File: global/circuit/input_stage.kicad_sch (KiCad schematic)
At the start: 9 parts, among them U3 TL081H

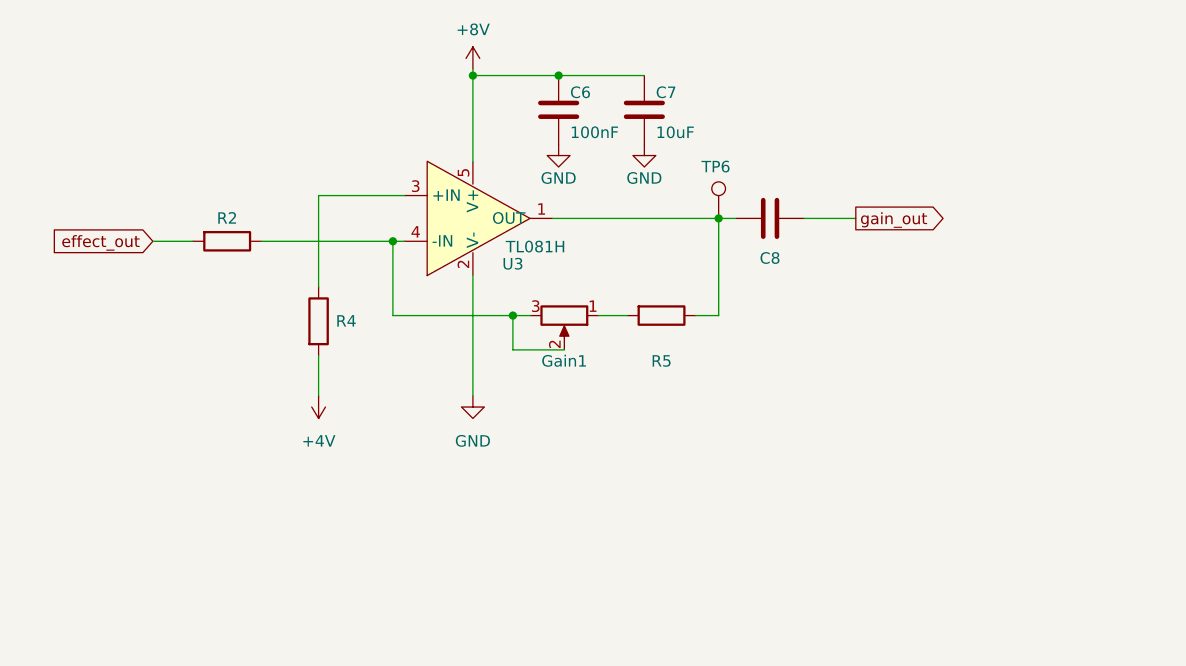
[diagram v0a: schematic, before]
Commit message: rework distortion circuit and simulations
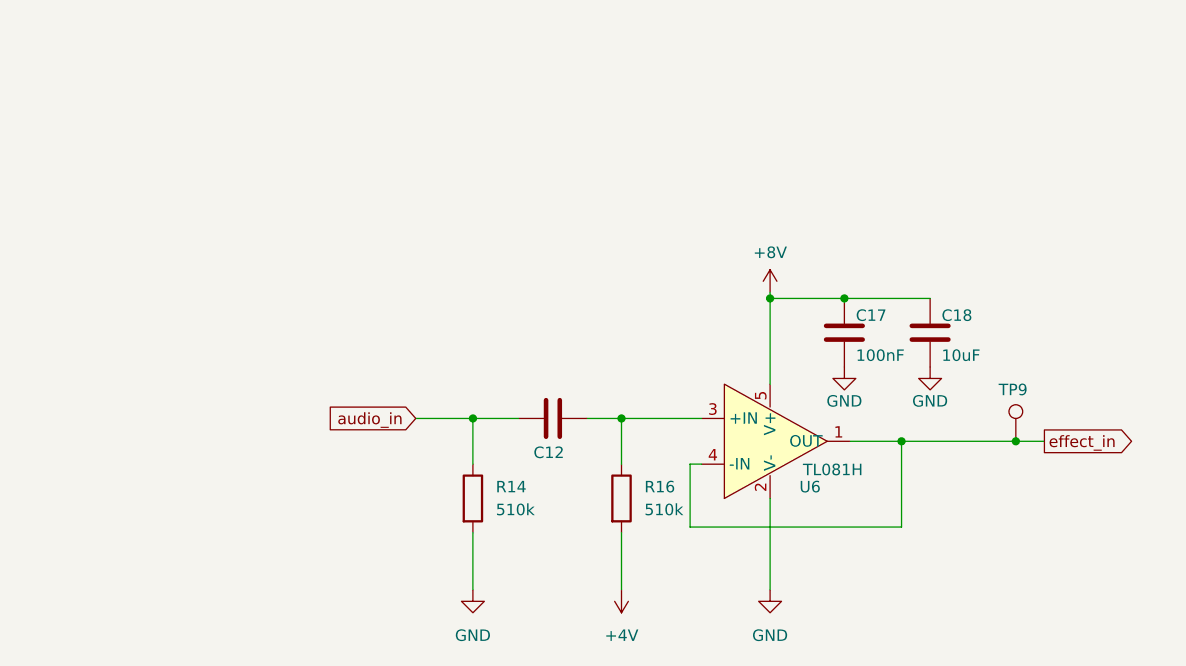
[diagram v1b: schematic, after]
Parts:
- removed C6: 100nF, Capacitor_SMD:C_0805_2012Metric_Pad1.18x1.45mm_HandSolder, symbol Device:C
- removed C7: 10uF, Capacitor_SMD:C_0805_2012Metric_Pad1.18x1.45mm_HandSolder, symbol Device:C
- removed C8: C, Capacitor_SMD:C_0805_2012Metric_Pad1.18x1.45mm_HandSolder, symbol Device:C
- removed Gain1: 10k, Connector_PinHeader_2.54mm:PinHeader_1x03_P2.54mm_Vertical, symbol Device:R_Potentiometer
- removed R2, R4, R5: R, Resistor_SMD:R_0805_2012Metric_Pad1.20x1.40mm_HandSolder, symbol Device:R
- removed TP6: TestPoint, TestPoint:TestPoint_THTPad_1.0x1.0mm_Drill0.5mm, symbol Connector:TestPoint
- removed U3: TL081H, Package_TO_SOT_SMD:SOT-23-5_HandSoldering, symbol Amplifier_Operational:TL081H
- added C12: 22uF, Capacitor_SMD:C_1206_3216Metric_Pad1.33x1.80mm_HandSolder, symbol Device:C
- added C17: 100nF, Capacitor_SMD:C_0805_2012Metric_Pad1.18x1.45mm_HandSolder, symbol Device:C
- added C18: 10uF, Capacitor_SMD:C_0805_2012Metric_Pad1.18x1.45mm_HandSolder, symbol Device:C
- added R14, R16: 510k, Resistor_SMD:R_0805_2012Metric_Pad1.20x1.40mm_HandSolder, symbol Device:R
- added TP9: TestPoint, TestPoint:TestPoint_THTPad_1.0x1.0mm_Drill0.5mm, symbol Connector:TestPoint
- added U6: TL081H, Package_TO_SOT_SMD:SOT-23-5_HandSoldering, symbol Amplifier_Operational:TL081H
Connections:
- net +4V: now also R16.2
- net +8V: now also C17.1, C18.1, U6.5 (V+)
- net GND: now also C17.2, C18.2, R14.2, U6.2 (V-)
- new net: C12.2, R16.1, U6.3 (+IN)
- new net audio_in: C12.1, R14.1
- new net effect_in: TP9.1, U6.1 (OUT), U6.4 (-IN)
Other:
- title: Gain Stage -> (none)

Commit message: create gerber files, update BOM for REV2
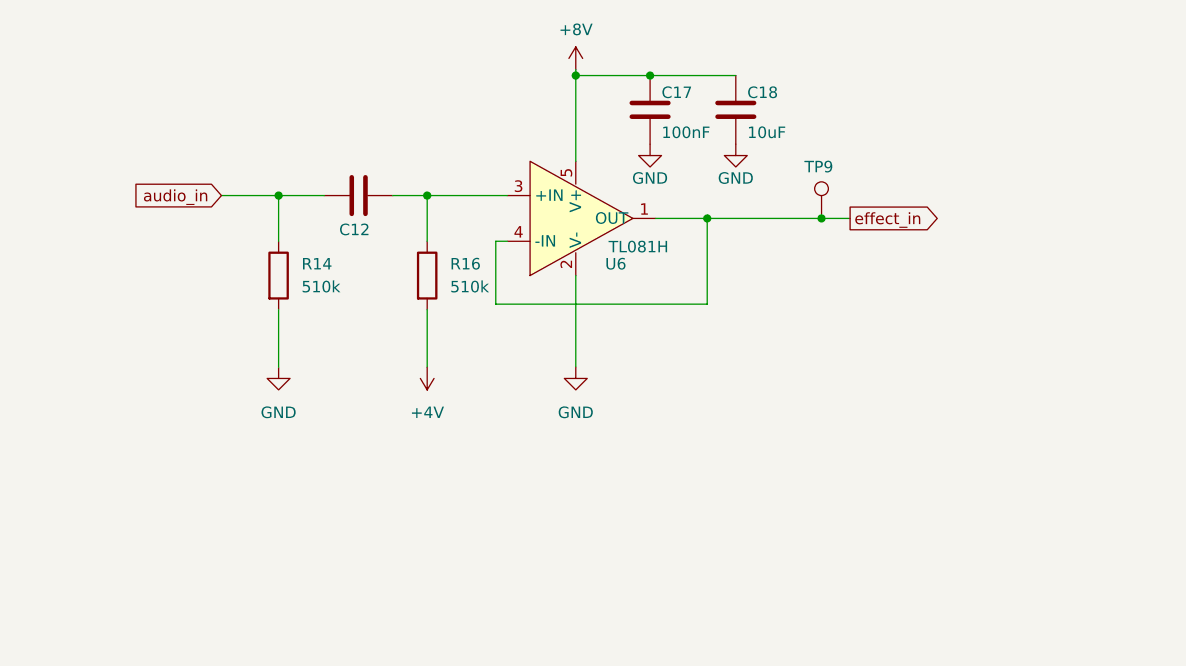
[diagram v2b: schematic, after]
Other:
- title: (none) -> Input stage
- moved on the sheet: C12, C17, C18, R14, R16, TP9, U6

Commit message: rework global circuits
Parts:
- renumbered C18 to C?, C17 to C?, C12 to C?, R16 to R?, R14 to R?, TP9 to TP?, U6 to U?
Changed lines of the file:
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@@
   (symbol (lib_id "power:+4V") (at 96.52 70.485 180) (unit 1)
     (in_bom yes) (on_board yes) (fields_autoplaced)
-    (property "Reference" "#PWR0116" (id 0) (at 96.52 66.675 0)
+    (property "Reference" "#PWR?" (id 0) (at 96.52 66.675 0)
       (effects (font (size 1.27 1.27)) hide)
     )
@@
   (symbol (lib_id "Device:C") (at 130.81 41.91 0) (unit 1)
     (in_bom yes) (on_board yes)
-    (property "Reference" "C18" (id 0) (at 132.08 40.005 0)
+    (property "Reference" "C?" (id 0) (at 132.08 40.005 0)
       (effects (font (size 1.27 1.27)) (justify left))
     )
@@
   (symbol (lib_id "Device:R") (at 96.52 60.325 0) (unit 1)
     (in_bom yes) (on_board yes) (fields_autoplaced)
-    (property "Reference" "R16" (id 0) (at 99.06 59.0549 0)
+    (property "Reference" "R?" (id 0) (at 99.06 59.0549 0)
       (effects (font (size 1.27 1.27)) (justify left))
     )
@@
   (symbol (lib_id "power:GND") (at 121.285 45.72 0) (unit 1)
     (in_bom yes) (on_board yes)
-    (property "Reference" "#PWR034" (id 0) (at 121.285 52.07 0)
+    (property "Reference" "#PWR?" (id 0) (at 121.285 52.07 0)
       (effects (font (size 1.27 1.27)) hide)
     )
@@
   (symbol (lib_id "Amplifier_Operational:TL081H") (at 113.03 53.975 0) (unit 1)
     (in_bom yes) (on_board yes)
-    (property "Reference" "U6" (id 0) (at 117.475 59.055 0))
+    (property "Reference" "U?" (id 0) (at 117.475 59.055 0))
     (property "Value" "TL081H" (id 1) (at 120.015 57.15 0))
     (property "Footprint" "Package_TO_SOT_SMD:SOT-23-5_HandSoldering" (id 2) (at 113.03 53.975 0)
@@
   (symbol (lib_id "power:GND") (at 80.01 70.485 0) (unit 1)
     (in_bom yes) (on_board yes) (fields_autoplaced)
-    (property "Reference" "#PWR029" (id 0) (at 80.01 76.835 0)
+    (property "Reference" "#PWR?" (id 0) (at 80.01 76.835 0)
       (effects (font (size 1.27 1.27)) hide)
     )
@@
   (symbol (lib_id "power:+8V") (at 113.03 37.465 0) (unit 1)
     (in_bom yes) (on_board yes)
-    (property "Reference" "#PWR032" (id 0) (at 113.03 41.275 0)
+    (property "Reference" "#PWR?" (id 0) (at 113.03 41.275 0)
       (effects (font (size 1.27 1.27)) hide)
     )
@@
   (symbol (lib_id "Connector:TestPoint") (at 140.335 53.975 0) (unit 1)
     (in_bom yes) (on_board yes)
-    (property "Reference" "TP9" (id 0) (at 138.43 48.26 0)
+    (property "Reference" "TP?" (id 0) (at 138.43 48.26 0)
       (effects (font (size 1.27 1.27)) (justify left))
     )
@@
   (symbol (lib_id "power:GND") (at 130.81 45.72 0) (unit 1)
     (in_bom yes) (on_board yes)
-    (property "Reference" "#PWR035" (id 0) (at 130.81 52.07 0)
+    (property "Reference" "#PWR?" (id 0) (at 130.81 52.07 0)
       (effects (font (size 1.27 1.27)) hide)
     )
@@
   (symbol (lib_id "Device:R") (at 80.01 60.325 0) (unit 1)
     (in_bom yes) (on_board yes) (fields_autoplaced)
-    (property "Reference" "R14" (id 0) (at 82.55 59.0549 0)
+    (property "Reference" "R?" (id 0) (at 82.55 59.0549 0)
       (effects (font (size 1.27 1.27)) (justify left))
     )
@@
   (symbol (lib_id "Device:C") (at 121.285 41.91 0) (unit 1)
     (in_bom yes) (on_board yes)
-    (property "Reference" "C17" (id 0) (at 122.555 40.005 0)
+    (property "Reference" "C?" (id 0) (at 122.555 40.005 0)
       (effects (font (size 1.27 1.27)) (justify left))
     )
@@
   (symbol (lib_id "power:GND") (at 113.03 70.485 0) (unit 1)
     (in_bom yes) (on_board yes) (fields_autoplaced)
-    (property "Reference" "#PWR033" (id 0) (at 113.03 76.835 0)
+    (property "Reference" "#PWR?" (id 0) (at 113.03 76.835 0)
       (effects (font (size 1.27 1.27)) hide)
     )
@@
   (symbol (lib_id "Device:C") (at 88.9 51.435 90) (unit 1)
     (in_bom yes) (on_board yes)
-    (property "Reference" "C12" (id 0) (at 90.17 55.245 90)
+    (property "Reference" "C?" (id 0) (at 90.17 55.245 90)
       (effects (font (size 1.27 1.27)) (justify left))
     )

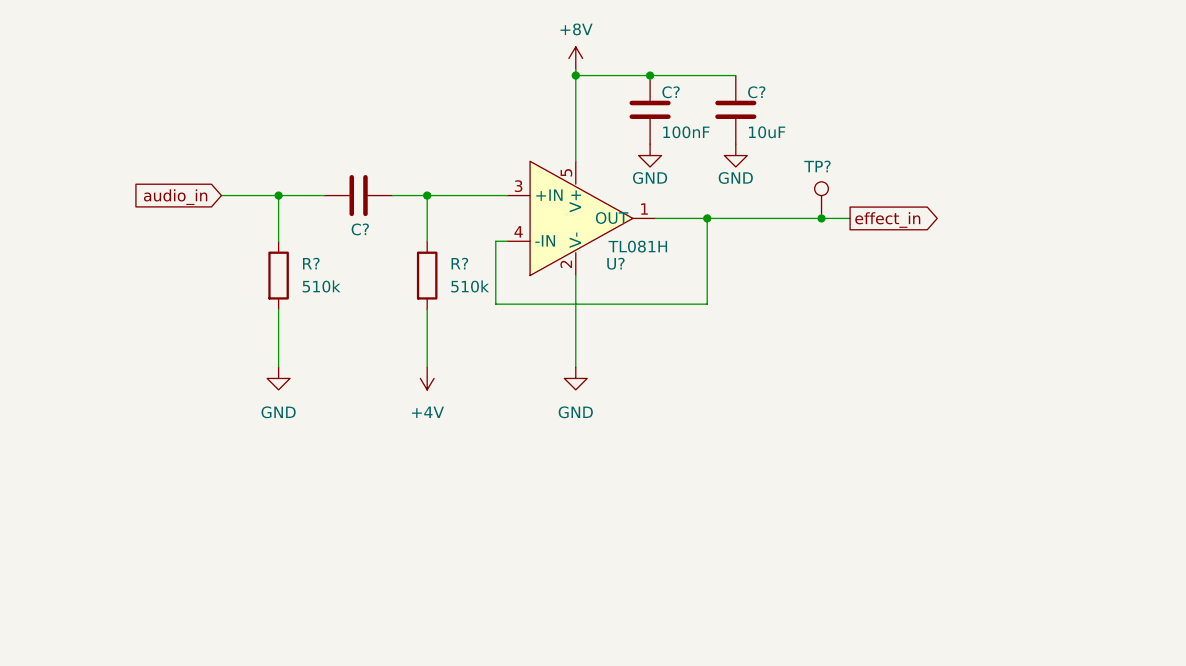
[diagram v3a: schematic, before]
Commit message: minor circuit rework for better use with multiple projects
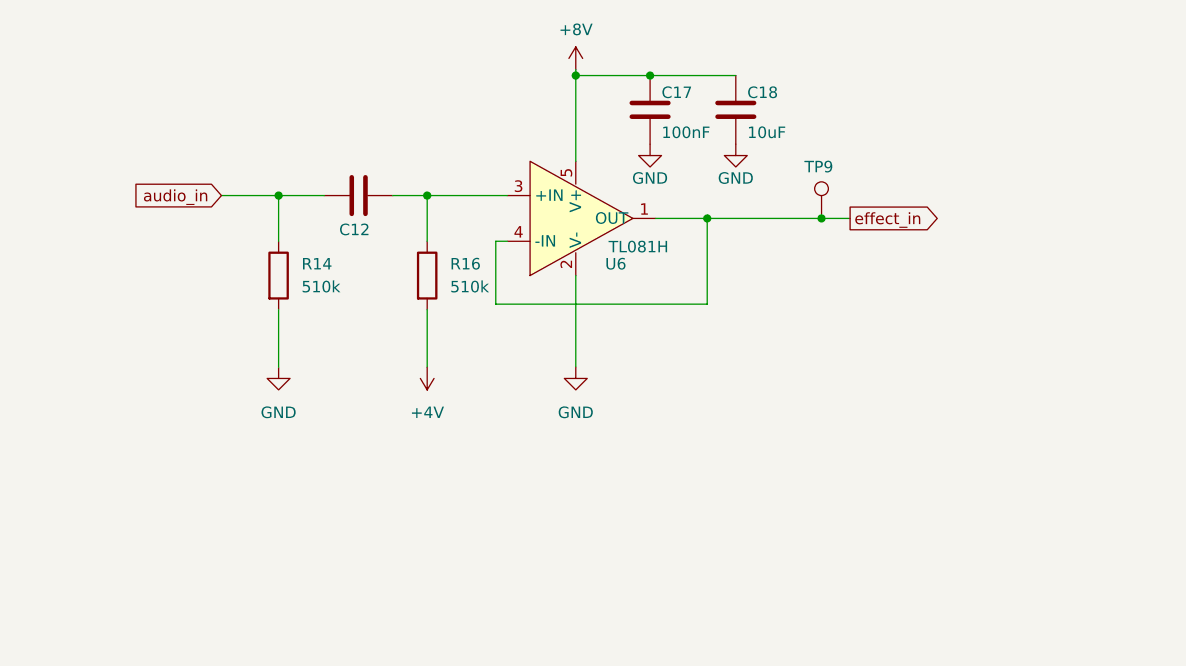
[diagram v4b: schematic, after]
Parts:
- gave numbers to parts that had none: 7
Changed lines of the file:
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@@
   (symbol (lib_id "power:+4V") (at 96.52 70.485 180) (unit 1)
     (in_bom yes) (on_board yes) (fields_autoplaced)
-    (property "Reference" "#PWR?" (id 0) (at 96.52 66.675 0)
+    (property "Reference" "#PWR0116" (id 0) (at 96.52 66.675 0)
       (effects (font (size 1.27 1.27)) hide)
     )
@@
   (symbol (lib_id "Device:C") (at 130.81 41.91 0) (unit 1)
     (in_bom yes) (on_board yes)
-    (property "Reference" "C?" (id 0) (at 132.08 40.005 0)
+    (property "Reference" "C18" (id 0) (at 132.08 40.005 0)
       (effects (font (size 1.27 1.27)) (justify left))
     )
@@
   (symbol (lib_id "Device:R") (at 96.52 60.325 0) (unit 1)
     (in_bom yes) (on_board yes) (fields_autoplaced)
-    (property "Reference" "R?" (id 0) (at 99.06 59.0549 0)
+    (property "Reference" "R16" (id 0) (at 99.06 59.0549 0)
       (effects (font (size 1.27 1.27)) (justify left))
     )
@@
   (symbol (lib_id "power:GND") (at 121.285 45.72 0) (unit 1)
     (in_bom yes) (on_board yes)
-    (property "Reference" "#PWR?" (id 0) (at 121.285 52.07 0)
+    (property "Reference" "#PWR034" (id 0) (at 121.285 52.07 0)
       (effects (font (size 1.27 1.27)) hide)
     )
@@
   (symbol (lib_id "Amplifier_Operational:TL081H") (at 113.03 53.975 0) (unit 1)
     (in_bom yes) (on_board yes)
-    (property "Reference" "U?" (id 0) (at 117.475 59.055 0))
+    (property "Reference" "U6" (id 0) (at 117.475 59.055 0))
     (property "Value" "TL081H" (id 1) (at 120.015 57.15 0))
     (property "Footprint" "Package_TO_SOT_SMD:SOT-23-5_HandSoldering" (id 2) (at 113.03 53.975 0)
@@
   (symbol (lib_id "power:GND") (at 80.01 70.485 0) (unit 1)
     (in_bom yes) (on_board yes) (fields_autoplaced)
-    (property "Reference" "#PWR?" (id 0) (at 80.01 76.835 0)
+    (property "Reference" "#PWR029" (id 0) (at 80.01 76.835 0)
       (effects (font (size 1.27 1.27)) hide)
     )
@@
   (symbol (lib_id "power:+8V") (at 113.03 37.465 0) (unit 1)
     (in_bom yes) (on_board yes)
-    (property "Reference" "#PWR?" (id 0) (at 113.03 41.275 0)
+    (property "Reference" "#PWR032" (id 0) (at 113.03 41.275 0)
       (effects (font (size 1.27 1.27)) hide)
     )
@@
   (symbol (lib_id "Connector:TestPoint") (at 140.335 53.975 0) (unit 1)
     (in_bom yes) (on_board yes)
-    (property "Reference" "TP?" (id 0) (at 138.43 48.26 0)
+    (property "Reference" "TP9" (id 0) (at 138.43 48.26 0)
       (effects (font (size 1.27 1.27)) (justify left))
     )
@@
   (symbol (lib_id "power:GND") (at 130.81 45.72 0) (unit 1)
     (in_bom yes) (on_board yes)
-    (property "Reference" "#PWR?" (id 0) (at 130.81 52.07 0)
+    (property "Reference" "#PWR035" (id 0) (at 130.81 52.07 0)
       (effects (font (size 1.27 1.27)) hide)
     )
@@
   (symbol (lib_id "Device:R") (at 80.01 60.325 0) (unit 1)
     (in_bom yes) (on_board yes) (fields_autoplaced)
-    (property "Reference" "R?" (id 0) (at 82.55 59.0549 0)
+    (property "Reference" "R14" (id 0) (at 82.55 59.0549 0)
       (effects (font (size 1.27 1.27)) (justify left))
     )
@@
   (symbol (lib_id "Device:C") (at 121.285 41.91 0) (unit 1)
     (in_bom yes) (on_board yes)
-    (property "Reference" "C?" (id 0) (at 122.555 40.005 0)
+    (property "Reference" "C17" (id 0) (at 122.555 40.005 0)
       (effects (font (size 1.27 1.27)) (justify left))
     )
@@
   (symbol (lib_id "power:GND") (at 113.03 70.485 0) (unit 1)
     (in_bom yes) (on_board yes) (fields_autoplaced)
-    (property "Reference" "#PWR?" (id 0) (at 113.03 76.835 0)
+    (property "Reference" "#PWR033" (id 0) (at 113.03 76.835 0)
       (effects (font (size 1.27 1.27)) hide)
     )
@@
   (symbol (lib_id "Device:C") (at 88.9 51.435 90) (unit 1)
     (in_bom yes) (on_board yes)
-    (property "Reference" "C?" (id 0) (at 90.17 55.245 90)
+    (property "Reference" "C12" (id 0) (at 90.17 55.245 90)
       (effects (font (size 1.27 1.27)) (justify left))
     )
